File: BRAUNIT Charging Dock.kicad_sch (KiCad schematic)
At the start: 0 parts

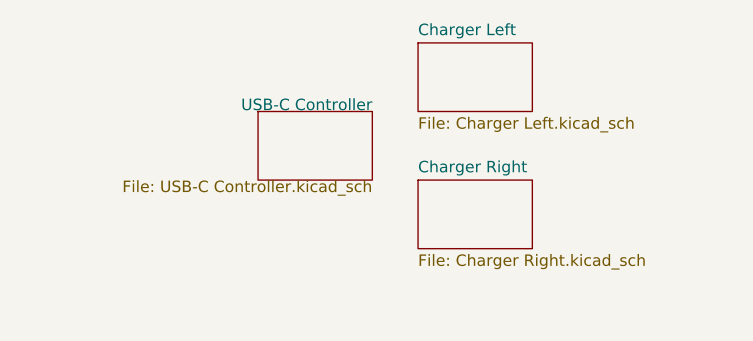
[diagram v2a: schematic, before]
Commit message: Change to 4-layer board and do some routing
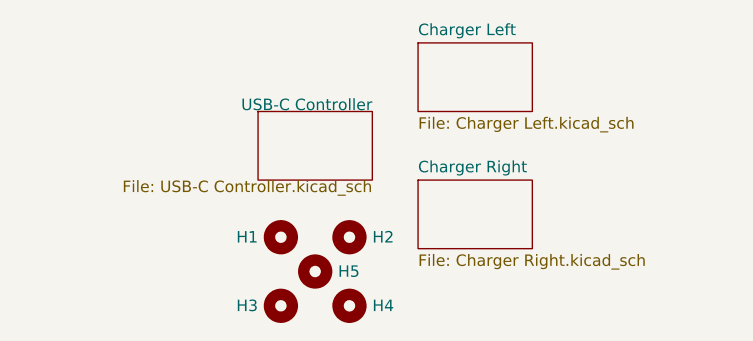
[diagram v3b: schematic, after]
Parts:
- added H1, H2, H3, H4, H5: (no value), symbol Mechanical:MountingHole
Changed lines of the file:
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@@
 (kicad_sch (version 20211123) (generator eeschema)
   (paper "A4")
+  (symbol (lib_id "Mechanical:MountingHole") (at 139.7 102.87 0) (unit 1)
+    (in_bom no) (on_board yes)
+    (property "Reference" "H1" (id 0) (at 137.16 102.87 0)
+      (effects (font (size 1.27 1.27)) (justify right))
+    )
+    (property "Value" "" (id 1) (at 142.24 104.1399 0)
+      (effects (font (size 1.27 1.27)) (justify left) hide)
+    )
+    (property "Footprint" "" (id 2) (at 139.7 102.87 0)
+      (effects (font (size 1.27 1.27)) hide)
+    )
+    (property "Datasheet" "~" (id 3) (at 139.7 102.87 0)
+      (effects (font (size 1.27 1.27)) hide)
+    )
+  )
+  (symbol (lib_id "Mechanical:MountingHole") (at 147.32 102.87 0) (unit 1)
+    (in_bom no) (on_board yes)
+    (property "Reference" "H2" (id 0) (at 149.86 102.87 0)
+      (effects (font (size 1.27 1.27)) (justify left))
+    )
+    (property "Value" "" (id 1) (at 149.86 104.1399 0)
+      (effects (font (size 1.27 1.27)) (justify left) hide)
+    )
+    (property "Footprint" "" (id 2) (at 147.32 102.87 0)
+      (effects (font (size 1.27 1.27)) hide)
+    )
+    (property "Datasheet" "~" (id 3) (at 147.32 102.87 0)
+      (effects (font (size 1.27 1.27)) hide)
+    )
+  )
+  (symbol (lib_id "Mechanical:MountingHole") (at 139.7 110.49 0) (unit 1)
+    (in_bom no) (on_board yes)
+    (property "Reference" "H3" (id 0) (at 137.16 110.49 0)
+      (effects (font (size 1.27 1.27)) (justify right))
+    )
+    (property "Value" "" (id 1) (at 142.24 111.7599 0)
+      (effects (font (size 1.27 1.27)) (justify left) hide)
+    )
+    (property "Footprint" "" (id 2) (at 139.7 110.49 0)
+      (effects (font (size 1.27 1.27)) hide)
+    )
+    (property "Datasheet" "~" (id 3) (at 139.7 110.49 0)
+      (effects (font (size 1.27 1.27)) hide)
+    )
+  )
+  (symbol (lib_id "Mechanical:MountingHole") (at 147.32 110.49 0) (unit 1)
+    (in_bom no) (on_board yes)
+    (property "Reference" "H4" (id 0) (at 149.86 110.49 0)
+      (effects (font (size 1.27 1.27)) (justify left))
+    )
+    (property "Value" "" (id 1) (at 149.86 111.7599 0)
+      (effects (font (size 1.27 1.27)) (justify left) hide)
+    )
+    (property "Footprint" "" (id 2) (at 147.32 110.49 0)
+      (effects (font (size 1.27 1.27)) hide)
+    )
+    (property "Datasheet" "~" (id 3) (at 147.32 110.49 0)
+      (effects (font (size 1.27 1.27)) hide)
+    )
+  )
+  (symbol (lib_id "Mechanical:MountingHole") (at 143.51 106.68 0) (unit 1)
+    (in_bom no) (on_board yes)
+    (property "Reference" "H5" (id 0) (at 146.05 106.68 0)
+      (effects (font (size 1.27 1.27)) (justify left))
+    )
+    (property "Value" "" (id 1) (at 146.05 107.9499 0)
+      (effects (font (size 1.27 1.27)) (justify left) hide)
+    )
+    (property "Footprint" "" (id 2) (at 143.51 106.68 0)
+      (effects (font (size 1.27 1.27)) hide)
+    )
+    (property "Datasheet" "~" (id 3) (at 143.51 106.68 0)
+      (effects (font (size 1.27 1.27)) hide)
+    )
+  )
   (sheet (at 154.94 96.52) (size 12.7 7.62) (fields_autoplaced)
     (stroke (width 0.1524) (type solid) (color 0 0 0 0))
@@
     )
     (path "/7a6d3a70-dd46-4bb3-a764-a6a3c3bbb5ac/4006f202-1362-4670-adf0-4e5892206b65"
-      (reference "#PWR?") (unit 1) (value "GND") (footprint "")
+      (reference "#PWR0138") (unit 1) (value "GND") (footprint "")
     )
     (path "/b2909144-61aa-40b6-b4ee-631beaa2767a/9c4ca713-efc0-464c-a186-be30f9d06ebd"
@@
       (reference "D14") (unit 1) (value "MHS110RGBCT") (footprint "BRAUNIT Charger:LED_RGB_Meihua_MHS110RGBCT")
     )
+    (path "/4fef9522-5998-4606-969a-7a340f99be8a"
+      (reference "H1") (unit 1) (value "MountingHole") (footprint "BRAUNIT Charger:MountingHole_2.7mm_M2.5_DIN912_Keepout")
+    )
+    (path "/59c49c55-6c6d-471f-b166-5115d4ca7108"
+      (reference "H2") (unit 1) (value "MountingHole") (footprint "BRAUNIT Charger:MountingHole_2.7mm_M2.5_DIN912_Keepout")
+    )
+    (path "/9d95df17-28dd-48b2-8022-b76561d40fee"
+      (reference "H3") (unit 1) (value "MountingHole") (footprint "BRAUNIT Charger:MountingHole_2.7mm_M2.5_DIN912_Keepout")
+    )
+    (path "/a78d6641-e24d-44c7-af44-1349d82c3523"
+      (reference "H4") (unit 1) (value "MountingHole") (footprint "BRAUNIT Charger:MountingHole_2.7mm_M2.5_DIN912_Keepout")
+    )
+    (path "/ba8244e2-67ae-47d6-acea-927aaf267f1a"
+      (reference "H5") (unit 1) (value "MountingHole") (footprint "BRAUNIT Charger:MountingHole_2.7mm_M2.5_DIN912_Keepout")
+    )
     (path "/b2909144-61aa-40b6-b4ee-631beaa2767a/c26c255b-63aa-45c6-aa93-37832edf0301"

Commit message: Only output connections to go :)
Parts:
- H1, H2, H3, H4, H5: value (none) -> MountingHole; footprint (none) -> BRAUNIT Charger:MountingHole_2.7mm_M2.5_DIN912_Keepout
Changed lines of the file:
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@@
       (effects (font (size 1.27 1.27)) (justify right))
     )
-    (property "Value" "" (id 1) (at 142.24 104.1399 0)
+    (property "Value" "MountingHole" (id 1) (at 142.24 104.1399 0)
       (effects (font (size 1.27 1.27)) (justify left) hide)
     )
-    (property "Footprint" "" (id 2) (at 139.7 102.87 0)
+    (property "Footprint" "BRAUNIT Charger:MountingHole_2.7mm_M2.5_DIN912_Keepout" (id 2) (at 139.7 102.87 0)
       (effects (font (size 1.27 1.27)) hide)
     )
@@
       (effects (font (size 1.27 1.27)) (justify left))
     )
-    (property "Value" "" (id 1) (at 149.86 104.1399 0)
+    (property "Value" "MountingHole" (id 1) (at 149.86 104.1399 0)
       (effects (font (size 1.27 1.27)) (justify left) hide)
     )
-    (property "Footprint" "" (id 2) (at 147.32 102.87 0)
+    (property "Footprint" "BRAUNIT Charger:MountingHole_2.7mm_M2.5_DIN912_Keepout" (id 2) (at 147.32 102.87 0)
       (effects (font (size 1.27 1.27)) hide)
     )
@@
       (effects (font (size 1.27 1.27)) (justify right))
     )
-    (property "Value" "" (id 1) (at 142.24 111.7599 0)
+    (property "Value" "MountingHole" (id 1) (at 142.24 111.7599 0)
       (effects (font (size 1.27 1.27)) (justify left) hide)
     )
-    (property "Footprint" "" (id 2) (at 139.7 110.49 0)
+    (property "Footprint" "BRAUNIT Charger:MountingHole_2.7mm_M2.5_DIN912_Keepout" (id 2) (at 139.7 110.49 0)
       (effects (font (size 1.27 1.27)) hide)
     )
@@
       (effects (font (size 1.27 1.27)) (justify left))
     )
-    (property "Value" "" (id 1) (at 149.86 111.7599 0)
+    (property "Value" "MountingHole" (id 1) (at 149.86 111.7599 0)
       (effects (font (size 1.27 1.27)) (justify left) hide)
     )
-    (property "Footprint" "" (id 2) (at 147.32 110.49 0)
+    (property "Footprint" "BRAUNIT Charger:MountingHole_2.7mm_M2.5_DIN912_Keepout" (id 2) (at 147.32 110.49 0)
       (effects (font (size 1.27 1.27)) hide)
     )
@@
       (effects (font (size 1.27 1.27)) (justify left))
     )
-    (property "Value" "" (id 1) (at 146.05 107.9499 0)
+    (property "Value" "MountingHole" (id 1) (at 146.05 107.9499 0)
       (effects (font (size 1.27 1.27)) (justify left) hide)
     )
-    (property "Footprint" "" (id 2) (at 143.51 106.68 0)
+    (property "Footprint" "BRAUNIT Charger:MountingHole_2.7mm_M2.5_DIN912_Keepout" (id 2) (at 143.51 106.68 0)
       (effects (font (size 1.27 1.27)) hide)
     )
